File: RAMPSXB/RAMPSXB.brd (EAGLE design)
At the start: 129.5 x 73.5 mm, 97 parts, among them CN1 1X4-BIG, CN2 1X4-BIG, CN3 1X4-BIG, CN4 1X4-BIG, CN5 1X4-BIG, CN6 1X4-BIG, CN7 1X4-BIG, CN8 1X4-BIG, CN9 1X4-BIG, J1 1X2-3.5MM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

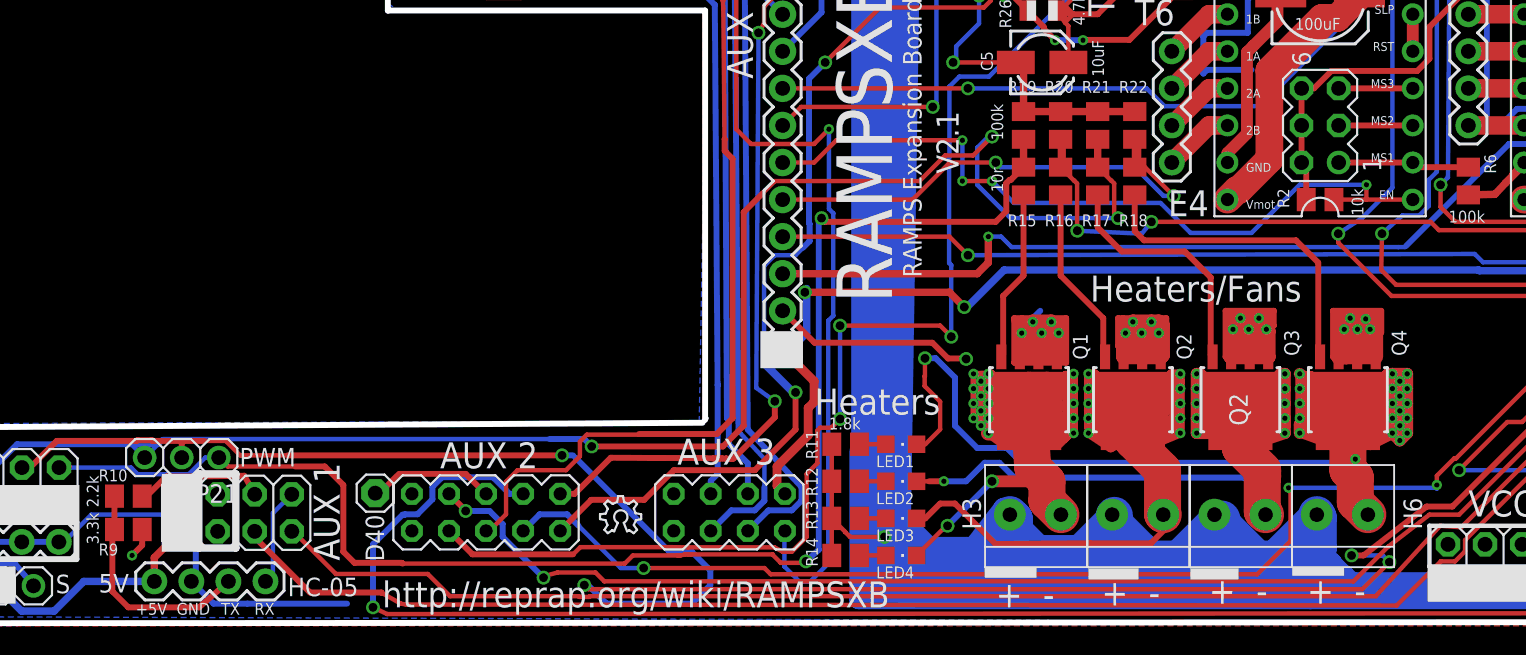
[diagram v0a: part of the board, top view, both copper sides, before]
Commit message: Expanded the traces on the FETs, corrected some incorrect pins on the infographic.
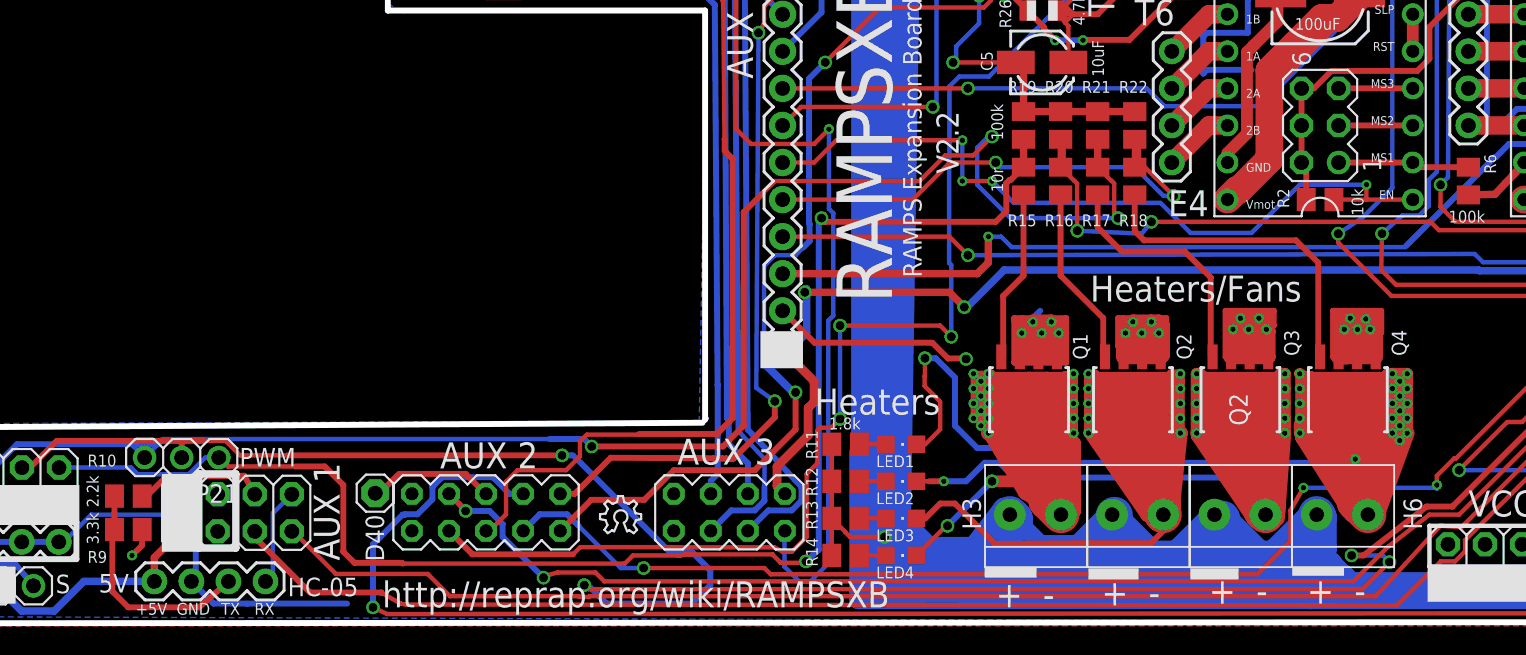
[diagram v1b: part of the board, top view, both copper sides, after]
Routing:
- net N$38: track 105.3 -> 136.4 mm
- net N$37: track 68.4 -> 97.5 mm
- net N$30: track 97.2 -> 124.0 mm
- net N$36: track 108.6 -> 133.2 mm
- net D44: track 123.2 -> 122.4 mm
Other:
- board text added: "V2.2"
- board text removed: "V2.1"

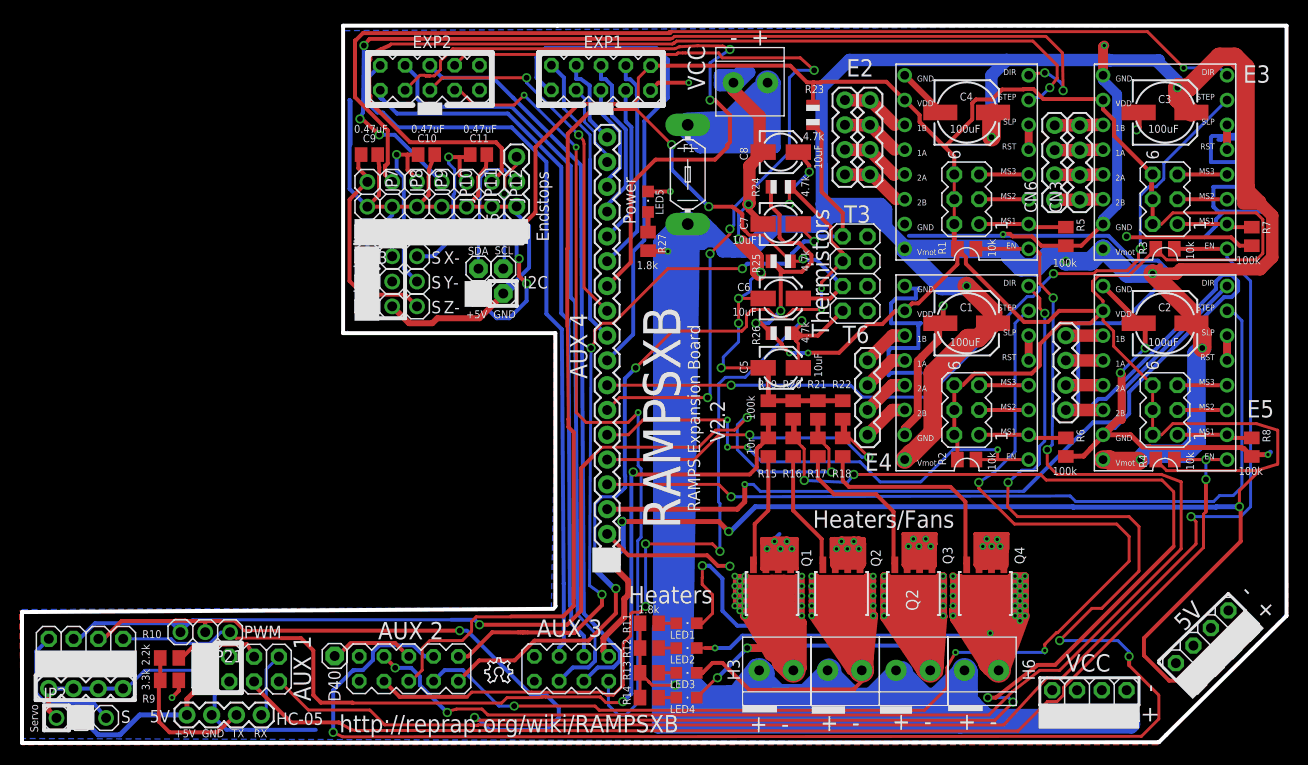
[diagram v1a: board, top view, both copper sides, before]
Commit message: Expanded Traces, Fixed Fonts
Changed Fonts to Vector, so they come out in the right place. Expanded
power traces.
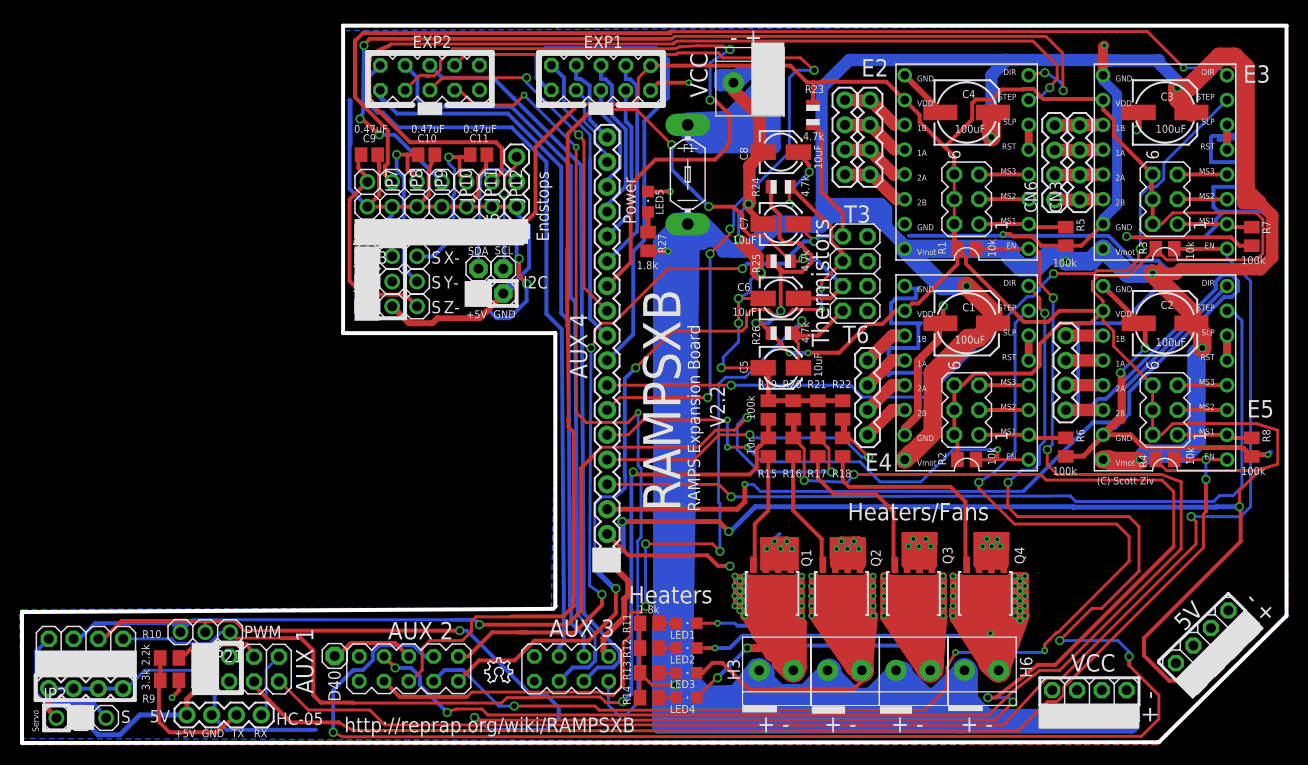
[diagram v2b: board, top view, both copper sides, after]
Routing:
- net N$38: track 136.4 -> 125.2 mm
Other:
- board text added: "(C) Scott Ziv"
- board text removed: "Q2"

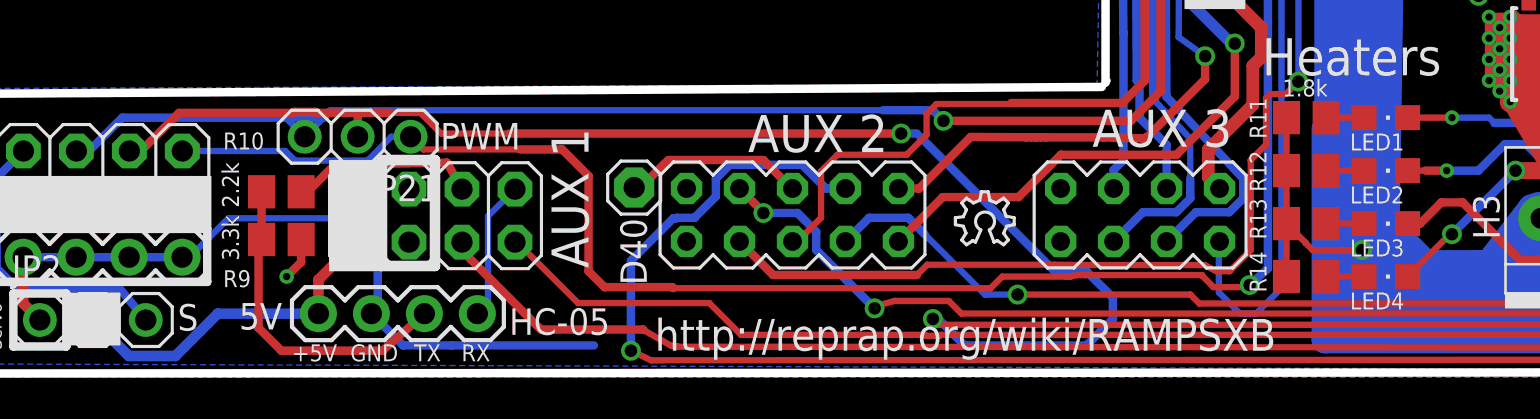
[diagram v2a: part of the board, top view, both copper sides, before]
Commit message: Fixed LED Numbering, updated V2.1
LED Indicators were not on the right FETs. Not sure how I missed that.
Updated V2.1 with corrected Vector Text.
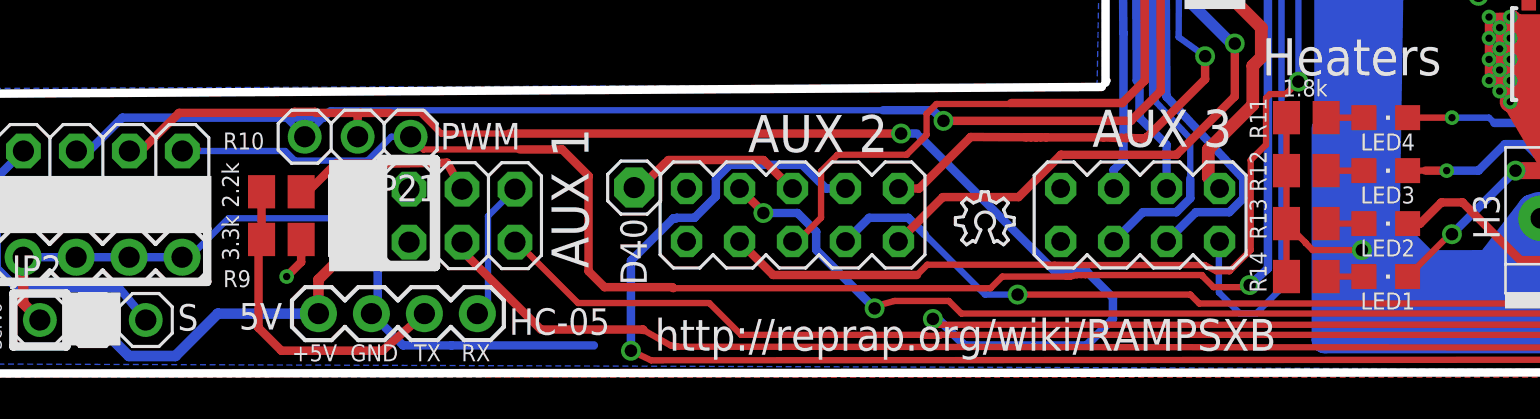
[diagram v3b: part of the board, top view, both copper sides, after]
